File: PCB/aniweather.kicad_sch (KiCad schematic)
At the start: 4 parts, among them SW1 SW_SPDT

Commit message: Further improvements
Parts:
- removed SW1: SW_SPDT, symbol Switch:SW_SPDT
- added BT1: Battery_Cell, TestPoint:TestPoint_2Pads_Pitch5.08mm_Drill1.3mm, symbol Device:Battery_Cell
- added SW1: SW_DIP_x01, Button_Switch_THT:SW_DIP_SPSTx01_Slide_9.78x4.72mm_W7.62mm_P2.54mm, symbol Switch:SW_DIP_x01
- added U3: ~, asylum:TP4056, symbol asylum:TP4056
- R1: footprint (none) -> Resistor_THT:R_Axial_DIN0207_L6.3mm_D2.5mm_P10.16mm_Horizontal
- U1: footprint (none) -> asylum:ST7735
- U2: footprint (none) -> asylum:C3 mini
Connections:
- net +3.3V: now also SW1.1, U3.2 (OUT+)
- net AO: now also U2.2 (A2); no longer U2.6
- net CS_LCD: now also U2.3 (A3); no longer U2.8
- net CS_SD: now also U2.7 (7/RGB_LED); no longer U2.10
- net GND: now also U3.3 (OUT-)
- net RESET: now also U2.4 (A4); no longer U2.3 (A3)
- net SCK: now also U2.1 (A1); no longer U2.7 (7/RGB_LED)
- net SD_MISO: now also U2.8; no longer U2.2 (A2)
- net SD_MOSI: now also U2.10; no longer U2.1 (A1)
- net at U2.12 (3.3V): now also SW1.2
- new net: BT1.1 (+), U3.0 (BAT+)
- new net: BT1.2 (-), U3.1 (BAT-)
- new net BAT_IN+: U3.4 (IN+)
- new net BAT_IN-: U3.5 (IN-)
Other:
- moved on the sheet: R1, U1, U2

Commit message: Saber plus PCB start
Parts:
- added C1, C2, C3, C4: Tiny, Capacitor_THT:C_Disc_D5.0mm_W2.5mm_P2.50mm, symbol Device:C
- added H1, H2, H3, H4: MountingHole, MountingHole:MountingHole_3.2mm_M3, symbol Mechanical:MountingHole
- added SW2: SW_Push, Button_Switch_THT:SW_PUSH_6mm, symbol Switch:SW_Push
- U2: footprint asylum:C3 mini -> asylum:WEMOS_C1_mini
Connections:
- net +3.3V: now also C1.2, C2.2, C3.2, C4.2, SW2.1
- net AO: now also U2.0 (A0); no longer U2.2 (A2)
- net CS_LCD: now also U2.2 (A2); no longer U2.3 (A3)
- net GND: now also C1.1, C2.1, C3.1, C4.1
- net RESET: now also U2.1 (A1); no longer U2.4 (A4)
- net SCK: now also U2.5 (A5); no longer U2.1 (A1)
- net SDA: now also U2.4 (A4)
- net SD_MISO: no longer U2.8
- net CS_SD: no longer names the net of U2.7 (7/RGB_LED)
- net CS_SD: no longer U1.8 (SD_CS)
- net SCL renamed SD_SCK
- new net SD_CS: U1.8 (SD_CS)
- no-connect marks 0 -> 3
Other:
- note added: "Battery module"
- note added: "LCD Module"
- note added: "Microcontroller module"

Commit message: V1.0
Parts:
- added C5: 0.1uF, Capacitor_THT:C_Disc_D5.0mm_W2.5mm_P2.50mm, symbol Device:C
- added C6, C7, C8: 10uF, Capacitor_THT:C_Disc_D5.0mm_W2.5mm_P2.50mm, symbol Device:C
- added L1: 2.2uH, Inductor_SMD:L_1210_3225Metric, symbol Device:L
- added R2: 100, Resistor_THT:R_Axial_DIN0207_L6.3mm_D2.5mm_P10.16mm_Horizontal, symbol Device:R
- added U5: TPS63001, Package_SON:Texas_DRC0010J_ThermalVias, symbol Regulator_Switching:TPS63001
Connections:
- net +3.3V: now also C4.1, C7.1, C8.1, U5.1 (VOUT), U5.10 (FB); no longer C3.2, C4.2, U3.2 (OUT+)
- net AO: now also U2.1 (A1); no longer U2.0 (A0)
- net CS_LCD: now also U2.3 (A3); no longer U2.2 (A2)
- net GND: now also C4.2, C5.2, C6.2, C7.2, C8.2, U5.11 (PGND), U5.3 (PGND), U5.9 (GND); no longer C3.1, C4.1
- net RESET: now also U2.2 (A2); no longer U2.1 (A1)
- net SCK: now also U2.4 (A4); no longer U2.5 (A5)
- net SDA: now also U2.0 (A0); no longer U2.4 (A4)
- net SD_CS: now also U2.10
- net SD_MISO: now also U2.7 (7/RGB_LED)
- net SD_MOSI: now also U2.8; no longer U2.10
- net SD_SCK: now also U2.6
- net at SW2.2: now also U2.5 (A5)
- net at BT1.1 (+), U3.0 (BAT+): now also C3.1
- net at BT1.2 (-), U3.1 (BAT-): now also C3.2
- new net: C5.1, R2.1, U5.6 (EN), U5.7 (PS/SYNC), U5.8 (VINA)
- new net: L1.1, U5.2 (L2)
- new net: L1.2, U5.4 (L1)
- new net: C6.1, R2.2, U3.2 (OUT+), U5.5 (VIN)
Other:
- moved on the sheet: BT1, C1, C2, C3, C4, SW2, U3

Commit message: Fix some small issues
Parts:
- added C9: Tiny, Capacitor_THT:C_Disc_D5.0mm_W2.5mm_P2.50mm, symbol Device:C
- added R3: 100k, Resistor_THT:R_Axial_DIN0207_L6.3mm_D2.5mm_P10.16mm_Horizontal, symbol Device:R
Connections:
- net +3.3V: now also U2.12 (3.3V), C9.1; no longer SW1.1, U2.11 (EN)
- net GND: now also C9.2, R3.1
- net at C6.1, R2.2, U5.5 (VIN): now also SW1.2; no longer U3.2 (OUT+)
- net at SW2.2, U2.5 (A5): now also R3.2
- net BAT_IN+: no longer names the net of U3.4 (IN+)
- net BAT_IN-: no longer names the net of U3.5 (IN-)
- new net: SW1.1, U3.2 (OUT+)
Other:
- moved on the sheet: C1, C2, C4, SW1

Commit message: Reroute board
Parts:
- added R4: 100k, Resistor_THT:R_Axial_DIN0207_L6.3mm_D2.5mm_P10.16mm_Horizontal, symbol Device:R
- added SW3: SW_Push, Button_Switch_THT:SW_PUSH_6mm, symbol Switch:SW_Push
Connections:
- net SD_SCK is gone; now on net SCK: U1.11 (SD_SCK), U2.6
- net +3.3V: now also SW3.1
- net CS_LCD: now also U2.10; no longer U2.3 (A3)
- net GND: now also R4.1
- net RESET: now also U2.3 (A3); no longer U2.2 (A2)
- net SCK: no longer U2.4 (A4)
- net SD_CS: now also U2.8; no longer U2.10
- net SDA: no longer names the net of U2.0 (A0)
- net SDA: now also R4.2, SW3.2; no longer U1.5 (SDA)
- net SD_MISO renamed MISO
- net MISO: now also U2.2 (A2); no longer U2.7 (7/RGB_LED)
- net SD_MOSI renamed MOSI
- net MOSI: now also U1.5 (SDA), U2.7 (7/RGB_LED); no longer U2.8
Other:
- moved on the sheet: R3, SW2, U2

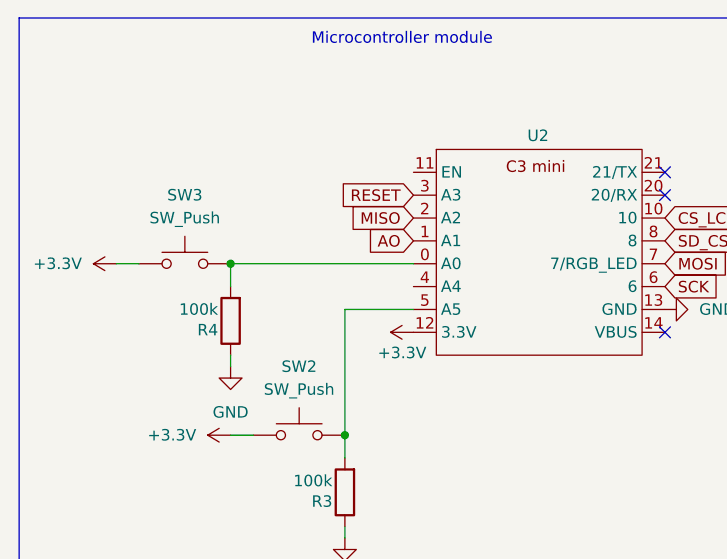
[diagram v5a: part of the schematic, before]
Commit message: Revisions for PCB and start of the firmware
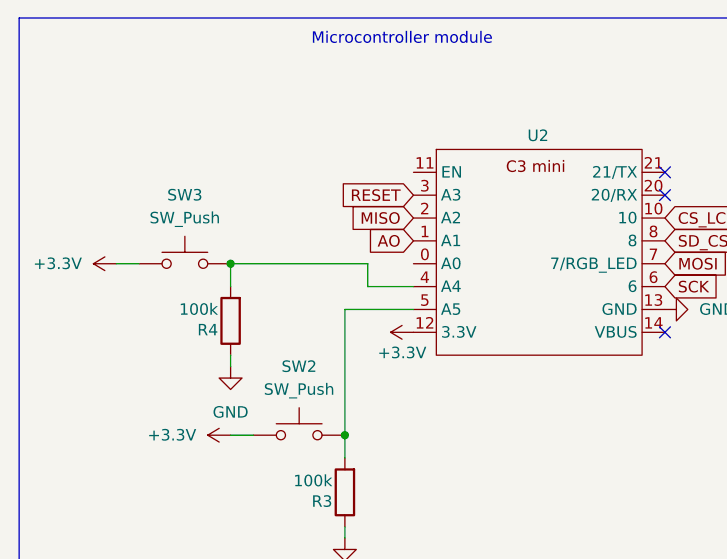
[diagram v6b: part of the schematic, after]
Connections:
- net at R4.2, SW3.2: now also U2.4 (A4); no longer U2.0 (A0)
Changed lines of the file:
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@@
+	)
+	(junction
+		(at 35.56 39.37)
+		(diameter 0)
+		(color 0 0 0 0)
 	)
 	(junction
@@
 	(junction
 		(at 267.97 46.99)
-		(diameter 0)
-		(color 0 0 0 0)
-	)
-	(junction
-		(at 35.56 39.37)
 		(diameter 0)
 		(color 0 0 0 0)
@@
 	(wire
 		(pts
+			(xy 50.8 41.91) (xy 55.88 41.91)
+		)
+		(stroke
+			(width 0)
+			(type default)
+		)
+	)
+	(wire
+		(pts
 			(xy 219.71 58.42) (xy 219.71 57.15)
 		)
@@
 	(wire
 		(pts
+			(xy 35.56 39.37) (xy 50.8 39.37)
+		)
+		(stroke
+			(width 0)
+			(type default)
+		)
+	)
+	(wire
+		(pts
 			(xy 35.56 39.37) (xy 35.56 41.91)
 		)
@@
 	(wire
 		(pts
-			(xy 35.56 39.37) (xy 55.88 39.37)
-		)
-		(stroke
-			(width 0)
-			(type default)
-		)
-	)
-	(wire
-		(pts
 			(xy 267.97 54.61) (xy 267.97 55.88)
 		)
@@
 		)
 		(stroke
+			(width 0)
+			(type default)
+		)
+	)
+	(wire
+		(pts
+			(xy 50.8 39.37) (xy 50.8 41.91)
+		)
+		(stroke
